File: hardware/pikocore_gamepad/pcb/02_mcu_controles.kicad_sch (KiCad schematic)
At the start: 11 parts, among them J4 ST7789_240x240, SW10 BTN_R, SW11 BTN_START, SW12 BTN_SELECT, SW13 NAV5, SW5 BTN_X, SW6 BTN_Y, SW7 BTN_A, SW8 BTN_B, SW9 BTN_L, U1 RP2350-Plus-16MB

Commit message: hw: D-pad de cuatro tacts 6x6 en lugar del NAV5, re-ruteo determinista del boost
El NAV5 de 5 vias es un solo actuador y no deja pulsar dos direcciones a la
vez, que es lo que piden Up+Down+B+A (reset de FX) y Down+Left+X+B (clock
lock). Vuelven SW1-SW4 (SW_PUSH_6mm) en cruz de 12.5mm centrada en X=30,
espejo del rombo; BTN_OK desaparece y GP26 queda libre con GP27/28; Start
pasa a x=26.75 para centrar su cuerpo en X=30. manual_tracks.py toma la lista
de tacts de netlist.TACTS, sin tercera copia. Tests, stub de firmware y doc
de pinout actualizados (196 tests).

Ruteo: freerouting 2.4.1 se lanza con -Djava.awt.headless=true -mt 1. Con
ventana, un NullPointerException en el repintado de AWT interrumpe el fanout
y el .ses sale con 60+ nets abiertas y exit 0. Las pistas manuales solo a
0/45/90 grados: con otro angulo la normalizacion oscila y aborta. Todo el
lazo del boost va ahora a mano y relativo a U2 (U2_5V hasta C5.1, C7_5V,
L1_VSYS_F, C4_VSYS_F): freerouting cerraba esos tramos una corrida si y
otra no. NPTH_KEEPOUT sube de 0.60 a 0.75 (BTN_R quedaba a 0.36mm del
anclaje de SW10).

Puertas: G-0/G-5/G-4/G-2/placement OK, ERC 0 errores (3 avisos GP26/27/28
reservados), DRC 0 errores / 0 abiertas / 0 paridad, G-F al dia, fab con las
4 capas (38 lineas de BOM, 17 sin LCSC: THT manuales y los 470uF).

Co-Authored-By: Claude Fable 5.1 <noreply@anthropic.com>
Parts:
- added SW2: DPAD_DOWN, Button_Switch_THT:SW_PUSH_6mm, symbol pikocore_gamepad:SW_Push
- added SW3: DPAD_LEFT, Button_Switch_THT:SW_PUSH_6mm, symbol pikocore_gamepad:SW_Push
- added SW4: DPAD_RIGHT, Button_Switch_THT:SW_PUSH_6mm, symbol pikocore_gamepad:SW_Push
- SW1: renamed from SW13; value NAV5 -> DPAD_UP; footprint gamesetup_lcsc:SW-TH_WS-1004-ARL10026 -> Button_Switch_THT:SW_PUSH_6mm; symbol pikocore_gamepad:NAV_WS1004 -> pikocore_gamepad:SW_Push; LCSC C42377836 -> (none)
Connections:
- net DPAD_DOWN: now also SW2.1 (A); no longer SW1.6 (DOWN)
- net DPAD_LEFT: now also SW3.1 (A); no longer SW1.2 (LEFT)
- net DPAD_RIGHT: now also SW4.1 (A); no longer SW1.5 (RIGHT)
- net DPAD_UP: now also SW1.1 (A); no longer SW1.4 (UP)
- net GND: now also SW1.2 (B), SW2.2 (B), SW3.2 (B), SW4.2 (B); no longer SW1.1 (COM)
- net BTN_OK renamed EXP_GP26
- net EXP_GP26: no longer SW1.3 (CENTER)
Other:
- note added: "Los 12 controles van DIRECTO a GPIO del modulo, sin expansor I2C. La asignacion esta en pinmap.py y la verifica la puerta G-4 contra el firmware. Los tacts de 6mm (SW1-SW8, SW11, SW12) tienen cuatro patas que son DOS PARES unidos dentro del switch; el simbolo declara 2 pines porque el footprint oficial de KiCad numera sus cuatro pads 1,1,2,2. Cablear 1 contra 2 ya cruza el contacto. SW9 y SW10 (g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"
- note removed: "Los 12 controles van DIRECTO a GPIO del modulo, sin expansor I2C. La asignacion esta en pinmap.py y la verifica la puerta G-4 contra el firmware. Los tacts de 6mm (SW5-SW8, SW11, SW12) tienen cuatro patas que son DOS PARES unidos dentro del switch; el simbolo declara 2 pines porque el footprint oficial de KiCad numera sus cuatro pads 1,1,2,2. Cablear 1 contra 2 ya cruza el contacto. SW9 y SW10 (g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"

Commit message: hw: pantalla por flex (DM-TFT13-377 24P + FPC 0.5mm) y layout del estudio ergonomico
El modulo LCD de 7 pines pasantes se reemplaza por el panel desnudo
DisplayModule DM-TFT13-377 variante 24 pines (LH133T-IF05, ST7789VW,
datasheet en hardware/pikocore_gamepad/datasheets/) pegado al frente, con
el FPC de 0.5mm al conector J4 XUNPU FPC-05FB-24PH20 (LCSC C2856831, huella
y STEP importados con easyeda2kicad). LCSC no tiene paneles de 1.3" en
stock y la variante de 12 pines usa FPC de 0.7mm, paso para el que LCSC no
vende conector. 4-SPI con IM=1, CS a masa (siempre seleccionado, como el
modulo), RD y DB0-7 a masa, TE a GP26 (LCD_TE). Backlight desde VSYS por
R21 (24R, perilla de brillo) y Q1 2N7002 (C8545) con R22 de pulldown;
C30/C31 de desacoplo. LCD1 es una huella sin pads generada por gen_fp.py
(origen = centro del area activa), DNP para el CPL pero en el BOM.

Layout segun el estudio ergonomico: panel con el BL a 3.0mm del borde
superior (area activa y 4.6-28), D-pad y rombo centrados en y 53.2 con paso
12.5, Select (50, 51) y Start (50, 63) apilados en la columna central, J4 en
(50, 44.6) rot 180 justo donde caen los contactos del flex desplegado,
R19/R20 bajados a y 72.5/75.5 por los pines de B. Los pulgares quedan 8mm
por debajo del vidrio; Up/X al costado de la franja sin vidrio.

G-0 queda ROJO a proposito: LCD_FPC_PIN_ORDER (V-8) no sale del datasheet
(lado de los contactos del FPC); se mide con el panel en mano y, si esta
espejado, J4 va a rot 0. gen_fab.py solo genera con --force hasta entonces.

Pipeline: plane_vias.py saltea el pad si hay una via propia a <0.6mm (los
13 GND del conector a 0.5mm daban hole_to_hole) y el fanout rechaza
candidatos pegados a una via de la misma net; finish_pcb.py borra stubs
colgantes. Tests reescritos para el panel (181). Puertas: G-5/G-4/G-2/
placement OK, 245 conexiones identicas, ERC 0 errores (2 avisos GP27/28),
DRC 0 errores / 0 abiertas / 0 paridad (10 avisos conocidos).

Co-Authored-By: Claude Fable 5.1 <noreply@anth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
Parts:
- added C30: 1uF, Capacitor_SMD:C_0603_1608Metric, symbol pikocore_gamepad:C
- added C31: 100nF, Capacitor_SMD:C_0603_1608Metric, symbol pikocore_gamepad:C
- added LCD1: DM-TFT13-377-24P, gamesetup_fp:LCD_LH133T_24P, symbol pikocore_gamepad:LCD_PANEL
- added Q1: 2N7002, Package_TO_SOT_SMD:SOT-23, symbol pikocore_gamepad:Q_NMOS
- added R21: 24R, Capacitor_SMD:C_0805_2012Metric, symbol pikocore_gamepad:R
- added R22: 100k, Resistor_SMD:R_0603_1608Metric, symbol pikocore_gamepad:R
- J4: value ST7789_240x240 -> LCD_FPC; footprint gamesetup_fp:LCD_ST7789_240x240_7P -> gamesetup_lcsc:FPC-SMD_24P-P0.50_FPC-05FB-24PH20; symbol pikocore_gamepad:LCD_ST7789 -> pikocore_gamepad:LCD_FPC24; LCSC (none) -> C2856831
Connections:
- net 3V3: now also J4.4 (VDD), J4.5 (VDDIO), J4.6 (IM), C30.1, C31.1; no longer J4.2 (VCC)
- net GND: now also J4.11 (RD), J4.13 (DB0), J4.14 (DB1), J4.15 (DB2), J4.16 (DB3), J4.17 (DB4), J4.18 (DB5), J4.19 (DB6), J4.20 (DB7), J4.23 (GND), J4.24 (GND), J4.25 (MP), J4.26 (MP), J4.3 (GND), J4.8 (CS), C30.2, C31.2, Q1.2 (S), R22.2; no longer J4.1 (GND)
- net LCD_BLK: now also Q1.1 (G), R22.1; no longer J4.7 (BLK)
- net LCD_DC: now also J4.10 (D/C); no longer J4.6 (DC)
- net LCD_MOSI: now also J4.12 (SDA); no longer J4.4 (SDA)
- net LCD_RES: now also J4.7 (RESET); no longer J4.5 (RES)
- net LCD_SCK: now also J4.9 (SCL); no longer J4.3 (SCL)
- net VSYS: now also R21.1
- net EXP_GP26 renamed LCD_TE
- net LCD_TE: now also J4.21 (TE)
- new net BL_A: J4.1 (LEDA), R21.2
- new net BL_K: J4.2 (LEDK), Q1.3 (D)
- no-connect marks 3 -> 4
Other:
- note added: "Los 12 controles van DIRECTO a GPIO del modulo, sin expansor I2C. La asignacion esta en pinmap.py y la verifica la puerta G-4 contra el firmware. PANTALLA: panel desnudo DM-TFT13-377 de 24 pines (ST7789VW) pegado al frente, FPC de 0.5mm al conector J4 (XUNPU FPC-05FB-24PH20, contactos de las dos caras). 4-SPI con IM=1 y CS A MASA (siempre seleccionado, como hacia el modulo de 7 pines): el bus SPI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"
- note removed: "Los 12 controles van DIRECTO a GPIO del modulo, sin expansor I2C. La asignacion esta en pinmap.py y la verifica la puerta G-4 contra el firmware. Los tacts de 6mm (SW1-SW8, SW11, SW12) tienen cuatro patas que son DOS PARES unidos dentro del switch; el simbolo declara 2 pines porque el footprint oficial de KiCad numera sus cuatro pads 1,1,2,2. Cablear 1 contra 2 ya cruza el contacto. SW9 y SW10 (g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"
- moved on the sheet: U1

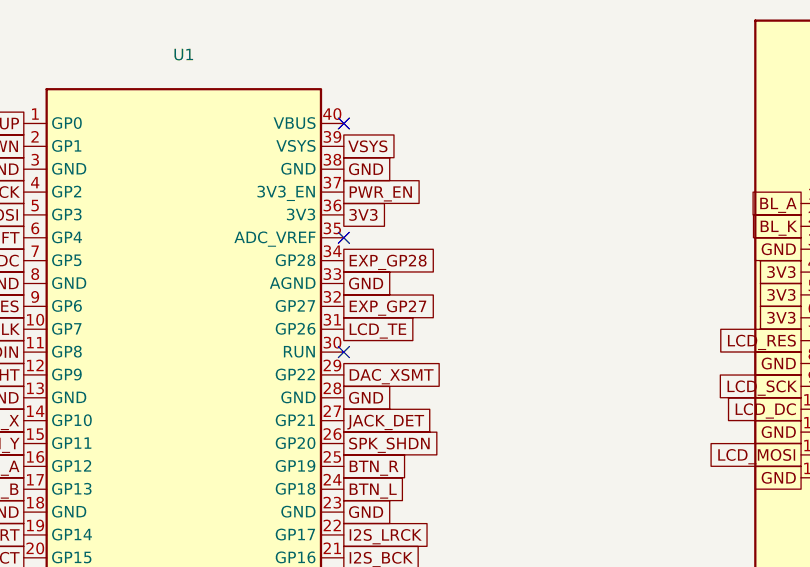
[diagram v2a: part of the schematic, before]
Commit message: hw: MIDI IN/OUT en TRS tipo A (hoja 07_midi, pinouts verificados)
Portado de hw/chipdown-rp2350: J6/J7 (TRS tipo A), U9 74LVC1G17, U10
H11L1SR2M, D3 1N4148W, R40-R43, C56, con la polaridad corregida (Ring ->
220R -> anodo del opto). TestMidi (9 tests), esquematico regenerado en seis
hojas y datasheets de TI SCES351Y y onsemi H11L1M rev 1.0.7.

Co-Authored-By: Claude Sonnet 5.5 <noreply@anthropic.com>
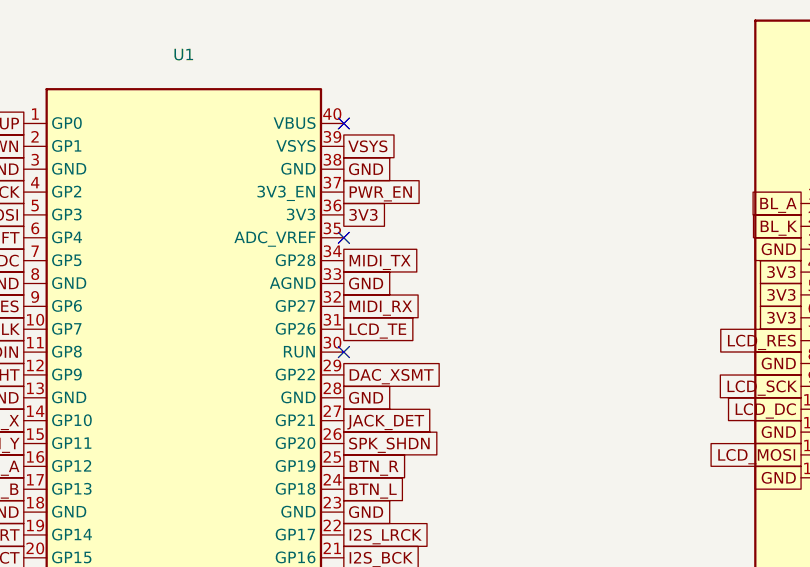
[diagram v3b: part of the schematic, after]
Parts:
- removed LCD1: DM-TFT13-377-24P, gamesetup_fp:LCD_LH133T_24P, symbol pikocore_gamepad:LCD_PANEL
- added C30: 1uF, Capacitor_SMD:C_0603_1608Metric, symbol pikocore_gamepad:C
- LCD1: renamed from C30; value 1uF -> DM-TFT13-377-24P; footprint Capacitor_SMD:C_0603_1608Metric -> gamesetup_fp:LCD_LH133T_24P; symbol pikocore_gamepad:C -> pikocore_gamepad:LCD_PANEL; LCSC C15849 -> (none); now not fitted
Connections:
- net 3V3: now also C30.1; no longer LCD1.1
- net GND: now also C30.2; no longer LCD1.2
- net EXP_GP27 renamed MIDI_RX
- net EXP_GP28 renamed MIDI_TX
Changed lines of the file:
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@@
     (date "2026-08-28")
     (rev "A")
-    (comment 1 "pikocore_gamepad - hoja 3 de 6")
+    (comment 1 "pikocore_gamepad - hoja 3 de 7")
     (comment 2 "Todas las conexiones son por GLOBAL LABEL: valen en todas las hojas")
   )
@@
     (property "Intersheetrefs" "${INTERSHEET_REFS}" (at 76.2 62.23 0) (effects (font (size 1.27 1.27)) (hide yes)))
   )
-  (global_label "EXP_GP27" (shape passive) (at 76.2 59.69 0)
+  (global_label "MIDI_RX" (shape passive) (at 76.2 59.69 0)
     (effects (font (size 1.27 1.27)) (justify left))
     (property "Intersheetrefs" "${INTERSHEET_REFS}" (at 76.2 59.69 0) (effects (font (size 1.27 1.27)) (hide yes)))
@@
     (property "Intersheetrefs" "${INTERSHEET_REFS}" (at 76.2 57.15 0) (effects (font (size 1.27 1.27)) (hide yes)))
   )
-  (global_label "EXP_GP28" (shape passive) (at 76.2 54.61 0)
+  (global_label "MIDI_TX" (shape passive) (at 76.2 54.61 0)
     (effects (font (size 1.27 1.27)) (justify left))
     (property "Intersheetrefs" "${INTERSHEET_REFS}" (at 76.2 54.61 0) (effects (font (size 1.27 1.27)) (hide yes)))

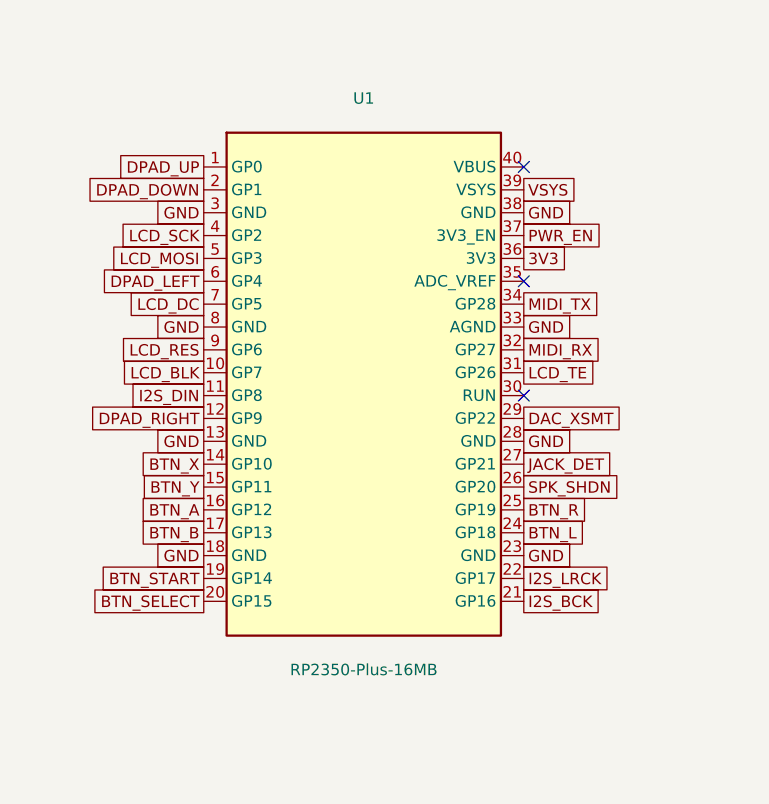
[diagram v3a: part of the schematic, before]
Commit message: hw: sin vias ni pasta bajo las pastillas del modulo
plane_vias.py ya no pone via en las pastillas de U1 (se sueldan a mano y
el taladro chupa el estano): la via va afuera de la caja de sus pastillas,
a 0.3mm del cobre, unida por un tramo en B.Cu. check_placement.py falla si
una via toca una pastilla de U1.

gen_fp.py quita la pasta sin nombre que la huella oficial traia para
D1-D3 (bajo el modulo el esten imprimiria bolitas). Test de las 40 pastas.

Esquematico y netlist regenerados (U1 ya con la huella castellated).

Co-Authored-By: Claude Opus 5.5 <noreply@anthropic.com>
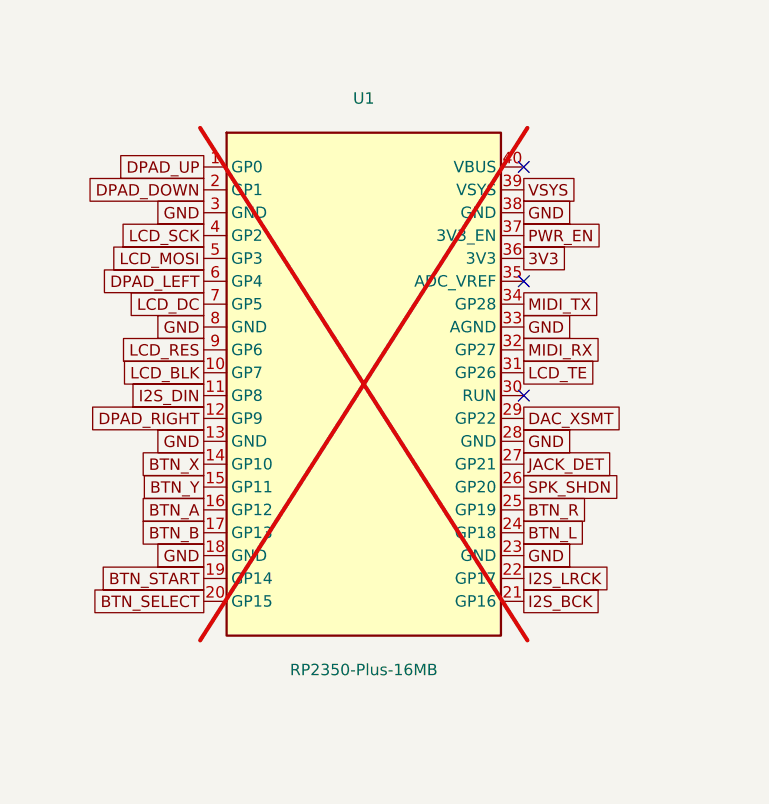
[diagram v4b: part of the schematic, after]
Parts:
- U1: footprint gamesetup_fp:RP2350-Plus_Socket -> gamesetup_fp:RP2350-Plus_Castellated; now not fitted
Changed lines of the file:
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@@
     (at 58.42 63.5 0)
     (unit 1)
-    (exclude_from_sim no) (in_bom yes) (on_board yes) (dnp no)
+    (exclude_from_sim no) (in_bom yes) (on_board yes) (dnp yes)
     (property "Reference" "U1" (at 58.42 31.75 0) (effects (font (size 1.27 1.27))))
     (property "Value" "RP2350-Plus-16MB" (at 58.42 95.25 0) (effects (font (size 1.27 1.27))))
-    (property "Footprint" "gamesetup_fp:RP2350-Plus_Socket" (at 58.42 63.5 0) (effects (font (size 1.27 1.27)) (hide yes)))
+    (property "Footprint" "gamesetup_fp:RP2350-Plus_Castellated" (at 58.42 63.5 0) (effects (font (size 1.27 1.27)) (hide yes)))
     (property "Datasheet" "https://www.waveshare.com/wiki/RP2350-Plus" (at 58.42 63.5 0) (effects (font (size 1.27 1.27)) (hide yes)))
     (property "Description" "Waveshare RP2350-Plus 16MB (RP2350A, cargador LiPo ETA6096, USB-C). Pin-compatible Raspberry Pi Pico, montado en socket 2x20. GP23/24/25 son internos del modulo y GP29 no sale al header." (at 58.42 63.5 0) (effects (font (size 1.27 1.27)) (hide yes)))
